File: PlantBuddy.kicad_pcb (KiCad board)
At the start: 4 copper layers, 44.3 x 29.2 mm, 74 parts, among them J1 USB_C_Receptacle_USB2.0, J101 JST, J102 Debug, J4 External, SW1 SW_Push, U1 LTR-303ALS-01, U101 AP2139AK-3.0TRG1, U102 nRF52832-QFAA, U104 XB5350A, U105 CN809T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

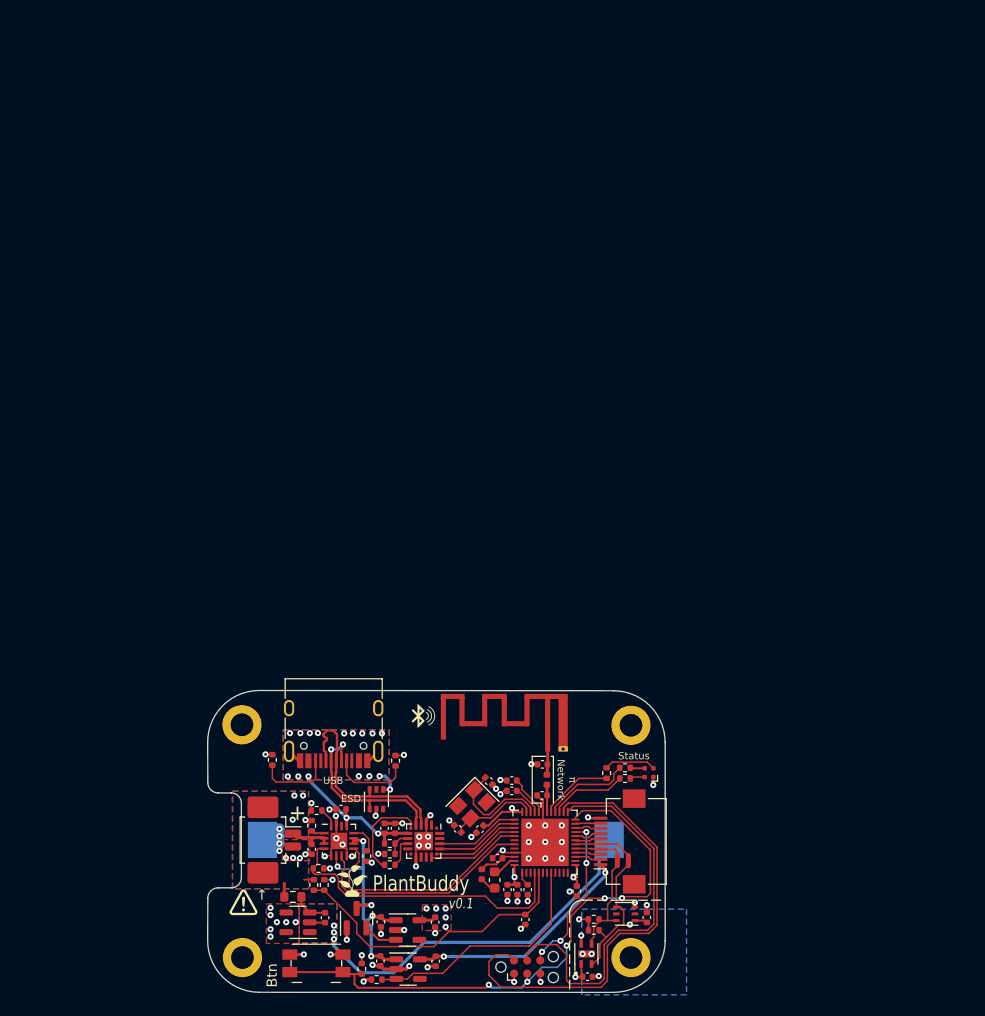
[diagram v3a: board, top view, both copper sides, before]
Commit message: Created and ordered a non-rechargeable version.
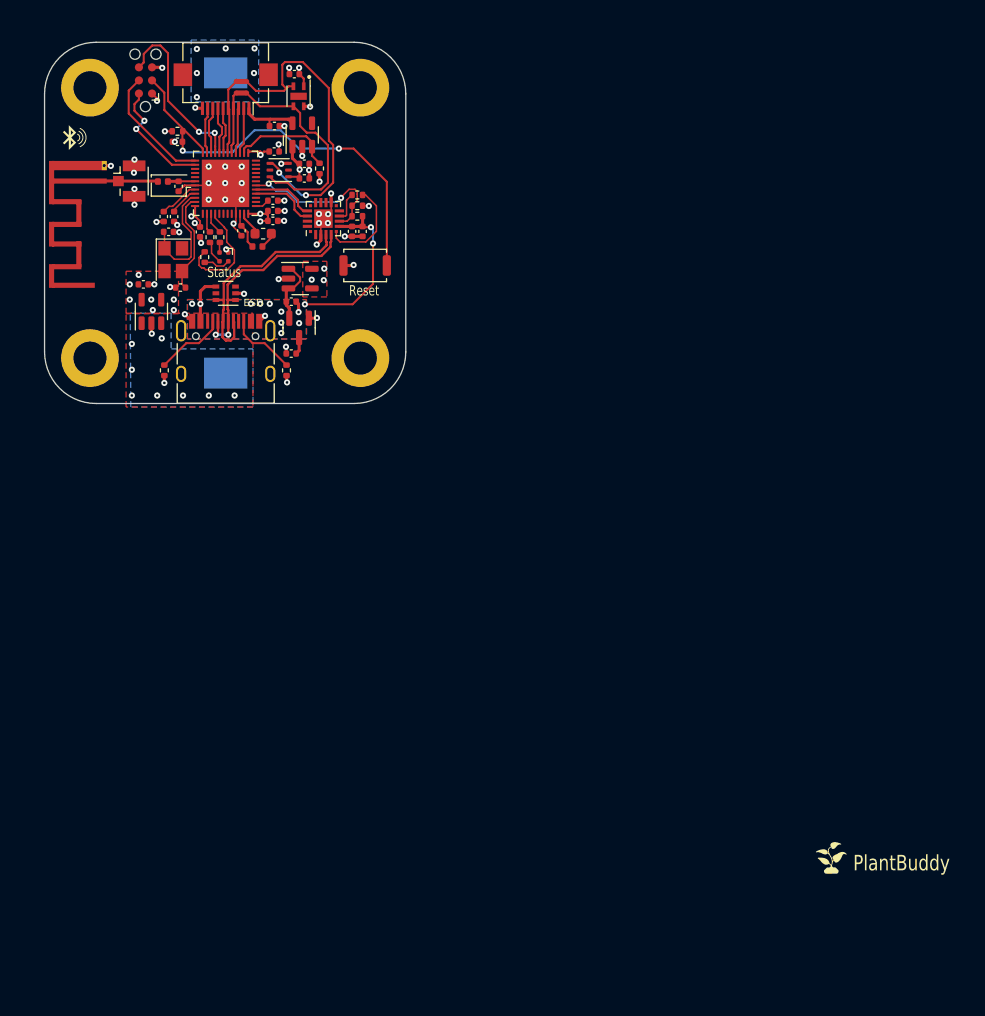
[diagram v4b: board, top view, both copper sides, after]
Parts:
- removed C10, C11: 4.7u, Capacitor_SMD:C_0402_1005Metric
- removed C103, C104: 100nF, Capacitor_SMD:C_0402_1005Metric
- removed C107: N/P, Capacitor_SMD:C_0402_1005Metric
- removed the G*** at (119.3, 133.3)
- removed J101: JST, Connector_Molex:Molex_PicoBlade_53261-0271_1x02-1MP_P1.25mm_Horizontal
- removed R10, R6, R9: 10k, Resistor_SMD:R_0402_1005Metric
- removed R103: 100R, Resistor_SMD:R_0603_1608Metric
- removed R13, R14: 1M, Resistor_SMD:R_0402_1005Metric
- removed R3, R4, R5: 5k1, Resistor_SMD:R_0402_1005Metric
- removed U101: AP2139AK-3.0TRG1, Package_TO_SOT_SMD:SOT-23-5
- removed U104: XB5350A, Package_TO_SOT_SMD:SOT-23-5
- removed U105: CN809T, Package_TO_SOT_SMD:SOT-23
- added C3: 1uF, Capacitor_SMD:C_0402_1005Metric, F.Cu at (123.9, 80.2)
- added C4: 1uF, Capacitor_SMD:C_0402_1005Metric, F.Cu at (123.9, 75.1)
- added J2: Conn_Coaxial, Connector_Coaxial:U.FL_Hirose_U.FL-R-SMT-1_Vertical, F.Cu at (108.2, 63.4)
- added U3: XC6206PxxxMR, Package_TO_SOT_SMD:SOT-23, F.Cu at (124.7, 77.7)
- added U6: MAX40203AUK+T, Package_TO_SOT_SMD:SOT-23-5, F.Cu at (124.8, 72.9)
- AE101: value Antenna_MIFA -> Antenna_IFA
- BT1: footprint Keystone-2450:KEYSTONE_1052TR -> PlantBuddy:BatteryHolder_LCSC_2032
- C6: value 4.7u -> 100nF
- H101, H102, H103, H104: footprint MountingHole:MountingHole_2.2mm_M2_DIN965_Pad -> MountingHole:MountingHole_3.2mm_M3_DIN965_Pad
- SW1: footprint Button_Switch_SMD:Panasonic_EVQPUK_EVQPUB -> Button_Switch_SMD:SW_Push_SPST_NO_Alps_SKRK
- U4: value BQ24072RGT -> MAX40203AUK+T; footprint Package_DFN_QFN:VQFN-16-1EP_3x3mm_P0.5mm_EP1.6x1.6mm -> Package_TO_SOT_SMD:SOT-23-5
- U5: value AP2139AK-3.0TRG1 -> MAX40203AUK+T
- moved J102 93.5 mm to (109.8, 53.7), turned to 90 degrees
- moved C2 92.0 mm to (124.2, 53.1), turned to 180 degrees
- moved U2 87.7 mm to (124.6, 55.2), turned to -90 degrees
- moved NT102 84.3 mm to (119.1, 53.8), turned to 180 degrees
- moved R108 83.1 mm to (112.9, 58.6), turned to 180 degrees
- moved NT101 82.8 mm to (119.1, 54.9), turned to 0 degrees
- moved C115 82.4 mm to (122.3, 58.1), turned to 0 degrees
- moved J4 82.3 mm to (117.6, 54.5), turned to 180 degrees
- moved U1 79.5 mm to (122.7, 62.4)
- moved C1 78.9 mm to (125.2, 63.2), turned to 0 degrees
- moved R101 78.8 mm to (126.6, 62.2), turned to 90 degrees
- moved U5 77.7 mm to (125.0, 59.0), turned to 90 degrees
- moved C101 77.6 mm to (125.2, 61.8), turned to 0 degrees
- moved C109 77.4 mm to (122.2, 60.6), turned to 0 degrees
- moved C117 71.2 mm to (122.1, 65.3), turned to 0 degrees
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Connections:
- net /FEED renamed /FEED2
- BT1 pad 1: +BATT -> /bat+
- BT1 pad 2: /Bat_n -> GND
- C101 pad 1: VCC -> +3V0
- C5 pad 1: VBUS -> +3V0
- C6 pad 1: GND -> /~{tRST}
- C6 pad 2: +BATT -> GND
- H103 pad 1: /Heat -> GND
- H104 pad 1: unconnected-(H104-Pad1) -> GND
- R104 pad 2: Net-(R104-Pad2) -> /USBDet
- R106 pad 1: Net-(R104-Pad2) -> /USBDet
- U102 pad 14: unconnected-(U102-Pad14) -> /S_EN
- U102 pad 27: /LED_R -> unconnected-(U102-Pad27)
- U102 pad 28: /LED_G -> unconnected-(U102-Pad28)
- U102 pad 29: /LED_B -> unconnected-(U102-Pad29)
- U102 pad 37: /UART_Rx -> unconnected-(U102-Pad37)
- U102 pad 38: /UART_Tx -> /LED_G
- U102 pad 39: /UART_CTS -> /LED_B
- U102 pad 4: /~{CHG_EN} -> /UART_Rx
- U102 pad 40: /UART_RTS -> /LED_R
- U102 pad 41: /~CHG -> unconnected-(U102-Pad41)
- U102 pad 43: /~PGOOD -> unconnected-(U102-Pad43)
- U102 pad 5: /batsense -> /UART_Tx
- U102 pad 6: unconnected-(U102-Pad6) -> /USBDet
- U102 pad 8: /S_EN -> unconnected-(U102-Pad8)
- U106 pad 15: /UART_RTS -> unconnected-(U106-Pad15)
- U106 pad 16: /UART_CTS -> unconnected-(U106-Pad16)
- U106 pad 8: Net-(R104-Pad2) -> /USBDet
- U2 pad 5: /Heat -> unconnected-(U2-Pad5)
- U4 pad 1: /Tsense -> /bat+
- U4 pad 2: +BATT -> GND
- U4 pad 3: +BATT -> /bat+
- U4 pad 4: /~{CHG_EN} -> (no net)
- U4 pad 5: GND -> +3V0
- U5 pad 1: VCC -> +3V0
- U5 pad 3: /PWR_EN -> /S_EN
- U5 pad 4: unconnected-(U5-Pad4) -> (no net)
- U5 pad 5: +3V0 -> /S_3V0
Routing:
- net /Bat_n: track 36.6 -> 0.00 mm, vias 3 -> 0
- net /SWDIO: track 44.5 -> 11.5 mm, vias 0 -> 2
- net /~{CHG_EN}: track 29.6 -> 0.00 mm
- net /batsense: track 29.3 -> 0.00 mm
- net /SWCLK: track 38.2 -> 11.9 mm
- net VCC: track 24.9 -> 0.00 mm, vias 5 -> 0
- net /~CHG: track 22.7 -> 0.00 mm
- net /~PGOOD: track 22.1 -> 0.00 mm
- net /SCL: track 13.2 -> 30.7 mm, vias 0 -> 2
- net /S_3V0: track 22.6 -> 5.81 mm, vias 2 -> 0
- net /~{tRST}: track 57.3 -> 41.9 mm, vias 5 -> 2
- net /USBDet: track 0.00 -> 15.3 mm, vias 0 -> 2
- net +BATT: track 14.4 -> 0.00 mm, vias 7 -> 0
- net /S_EN: track 23.6 -> 10.1 mm
- net GND: track 56.9 -> 43.5 mm, vias 70 -> 60
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- added copper zone on B.Cu, net /bat+
- added copper zone on F.Cu, net /bat+
- added copper zone on B.Cu, net GND
- removed copper zone on B.Cu, net +BATT
- removed copper zone on F.Cu, net +BATT
- removed copper zone on B.Cu, net /Bat_n
- removed copper zone on F.Cu, net /Bat_n
- removed copper zone on B.Cu, net /Heat
- removed copper zone on F.Cu, net GND
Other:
- board size 44.3 x 29.2 mm -> 35 x 35 mm
- board text added: "Reset"
- board text removed: "+"
- board text removed: "-"
- board text removed: "Btn"
- board text removed: "USB"
- board text removed: "v0.1"
- board text removed: "π Network"
- board text removed: "↑"

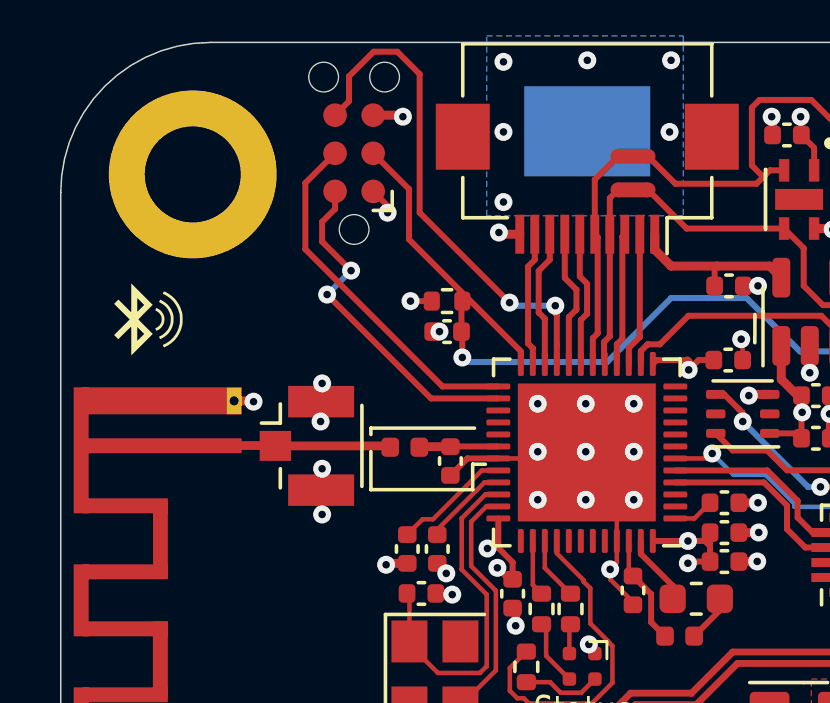
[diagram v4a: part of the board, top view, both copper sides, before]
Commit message: Updated coax connector placement
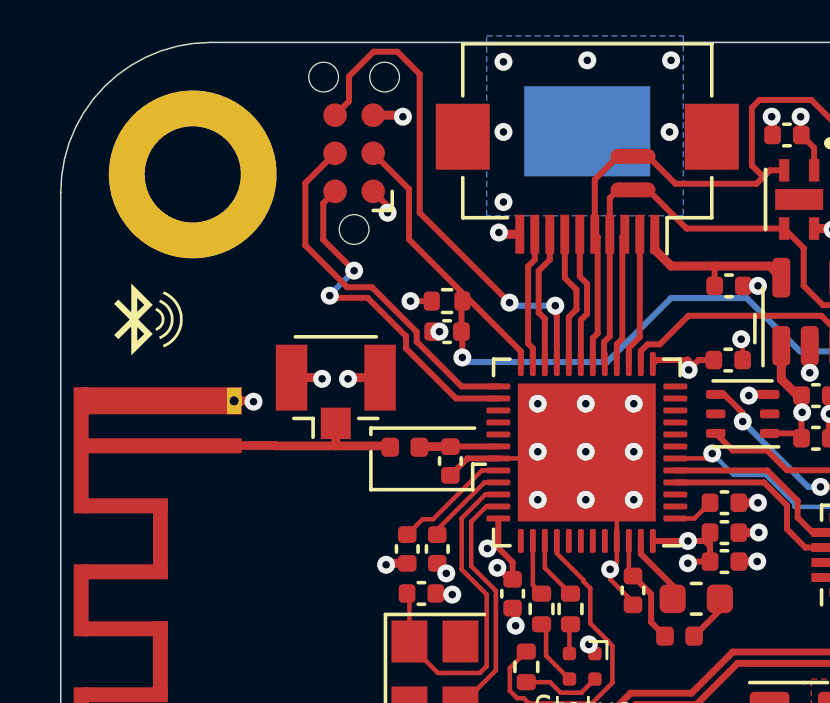
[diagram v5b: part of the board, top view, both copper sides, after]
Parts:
- moved J2 2.04 mm to (109.2, 61.6), turned to 90 degrees
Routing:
- net /FEED2: track 5.28 -> 6.03 mm
- net GND: track 43.5 -> 42.7 mm, vias 60 -> 58

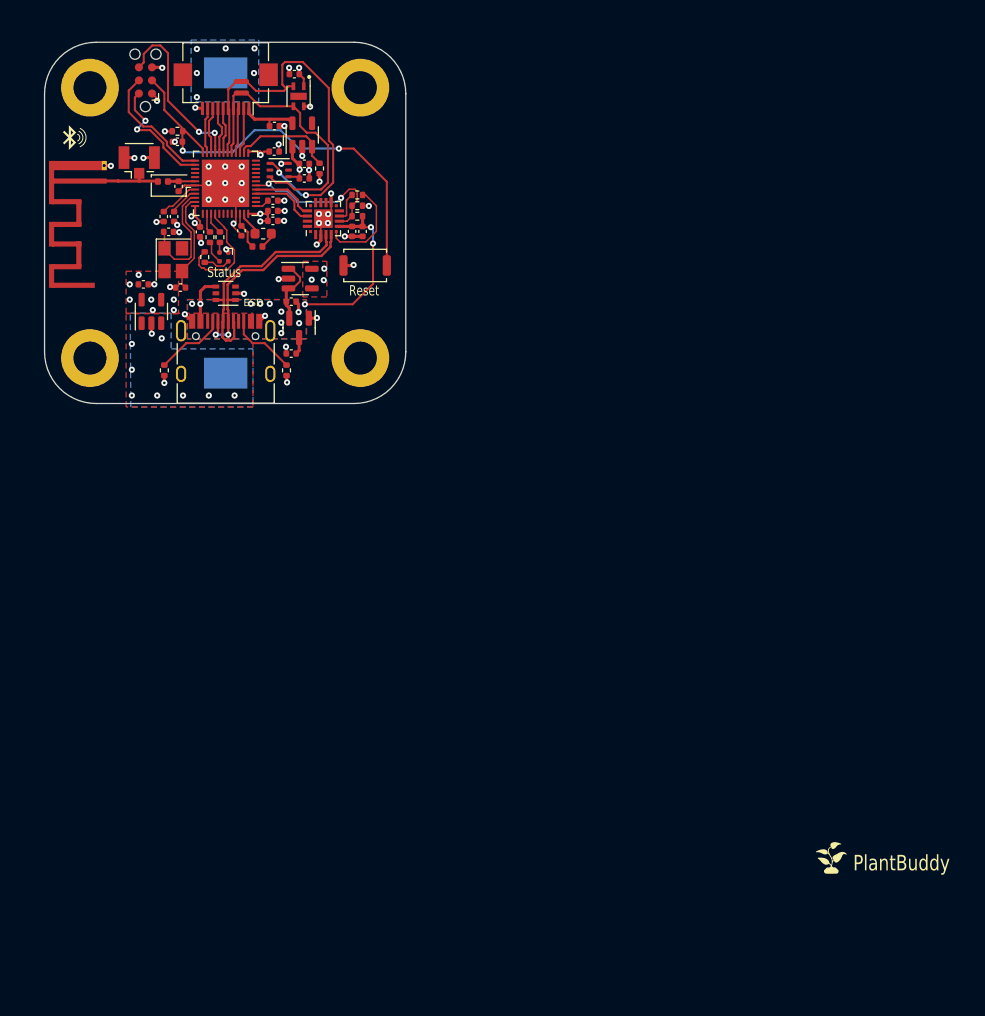
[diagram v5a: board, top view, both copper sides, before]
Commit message: Enhanced silkscreen layer.
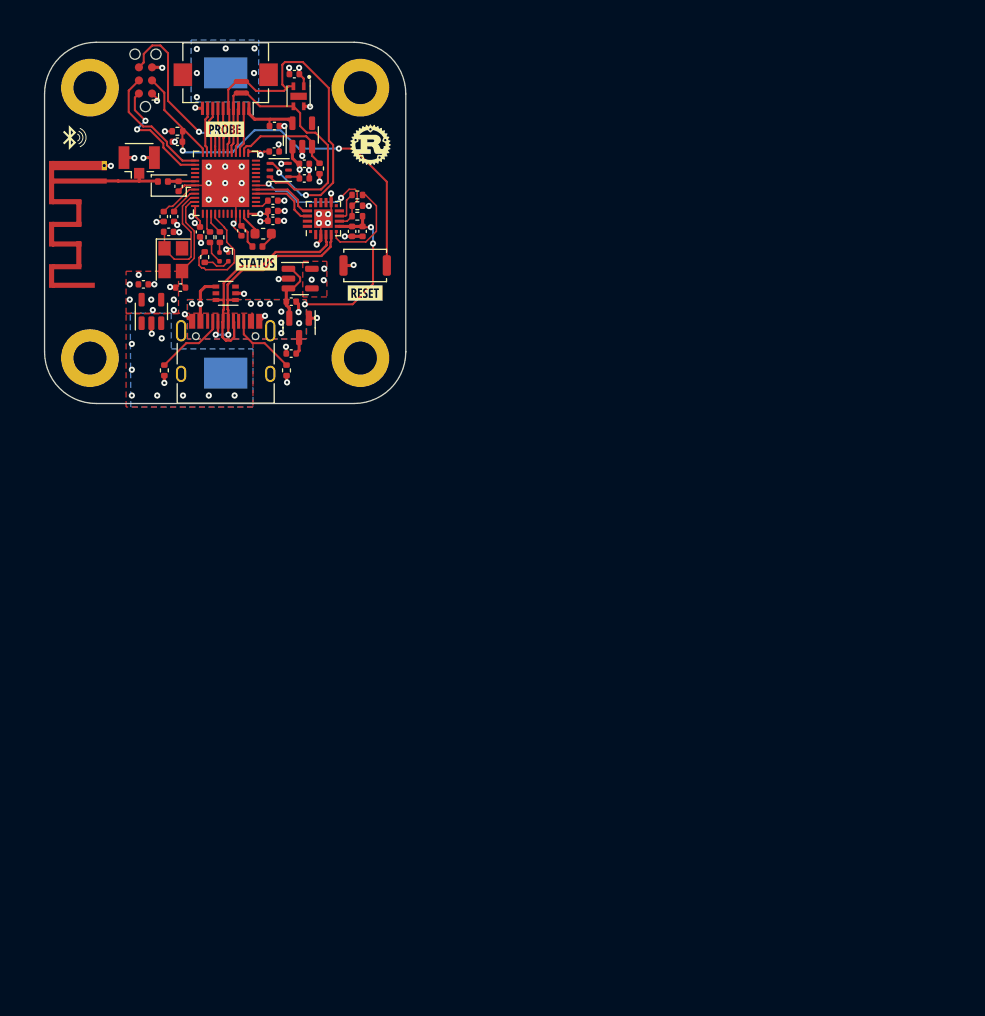
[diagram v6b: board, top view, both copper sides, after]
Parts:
- added G***: LOGO, LOGO, F.Cu at (120.5, 71.4)
- added G***: LOGO, LOGO, F.Cu at (131.1, 74.3)
- added G***: LOGO, LOGO, F.Cu at (131.6, 59.9)
- added G***: LOGO, LOGO, F.Cu at (117.5, 58.4)
- added G***: LOGO, LOGO, B.Cu at (103.1, 69.1)
- added G***: LOGO, LOGO, B.Cu at (131.4, 65.4)
- added G***: LOGO, LOGO, B.Cu at (131.4, 74.3)
- G***: moved to B.Cu
- moved G*** 100.1 mm to (102.9, 61.0), turned to -90 degrees
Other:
- board text removed: "ESD"
- board text removed: "PlantBuddy"
- board text removed: "Reset"
- board text removed: "Status"

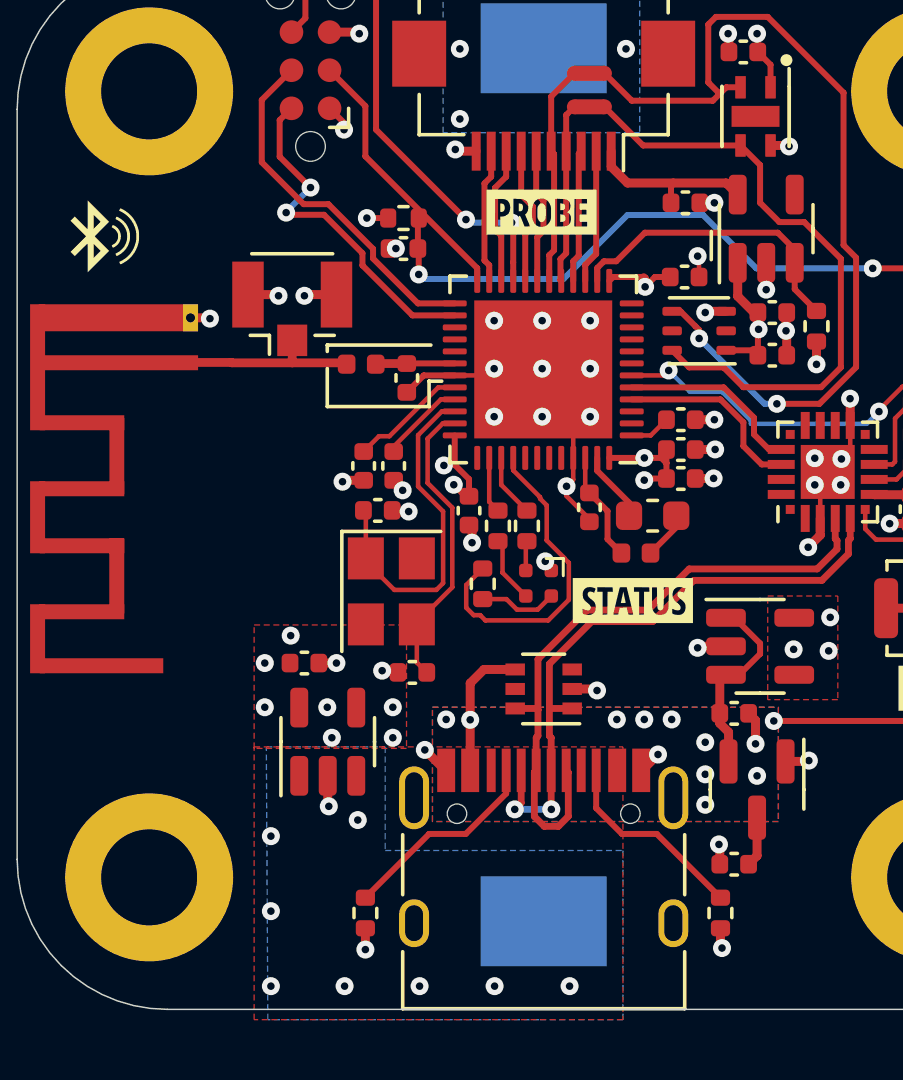
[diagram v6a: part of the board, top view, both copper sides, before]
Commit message: Fixed probe not working due to brownout
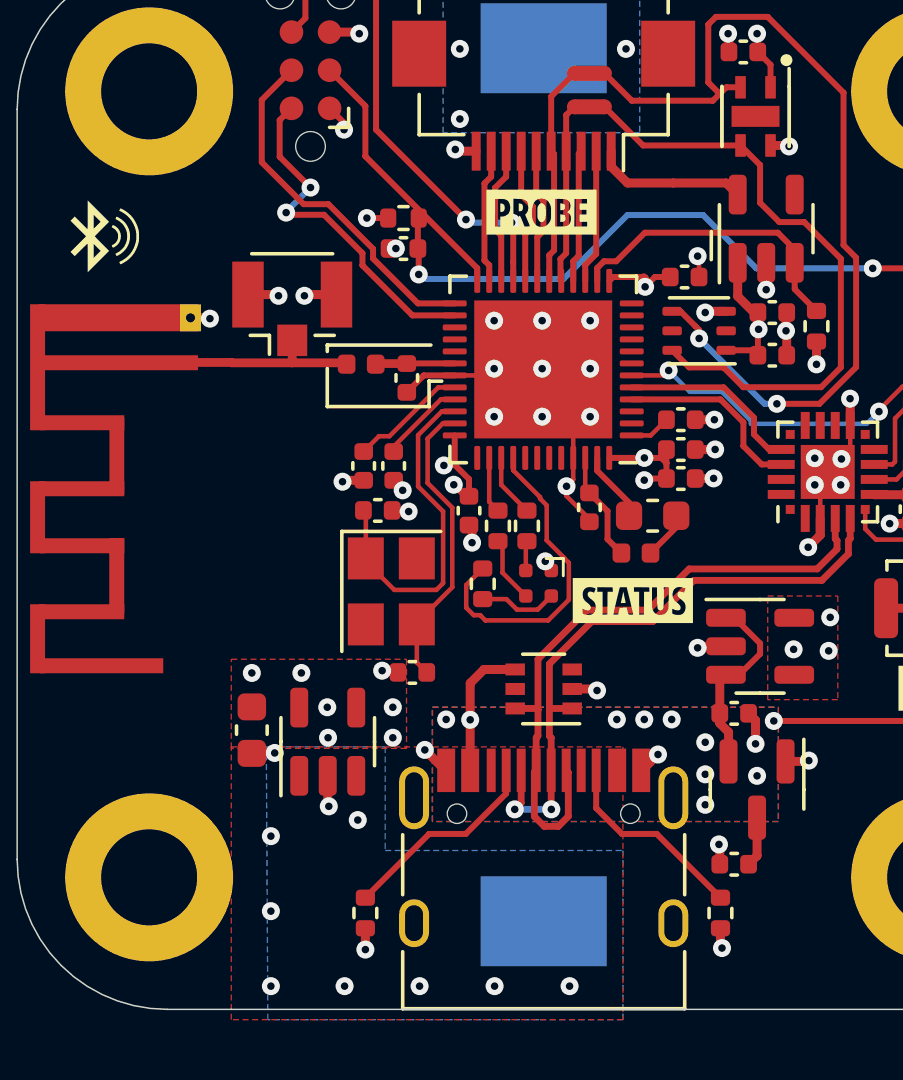
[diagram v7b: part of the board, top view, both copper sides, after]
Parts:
- removed C115: 4.7u, Capacitor_SMD:C_0402_1005Metric
- added G***: LOGO, LOGO, B.Cu at (105.7, 67.3)
- C3: value 1uF -> 4.7u
- C5: value 4.7u -> 22uF; footprint Capacitor_SMD:C_0402_1005Metric -> Capacitor_SMD:C_0603_1608Metric
- R106: value 47k -> 22k
- moved C5 2.84 mm to (107.8, 75.7), turned to -90 degrees
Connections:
- net /FEED2 renamed /FEED1
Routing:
- net /S_3V0: track 5.81 -> 5.12 mm
- net GND: track 42.7 -> 42.4 mm, vias 58 -> 57
- net +3V0: vias 20 -> 19
